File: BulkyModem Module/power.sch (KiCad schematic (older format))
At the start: 15 parts, among them J1 DC IN, J4 Conn_Power, K1 HK19F-DC, U2 74HCT04, U5 74HCT04

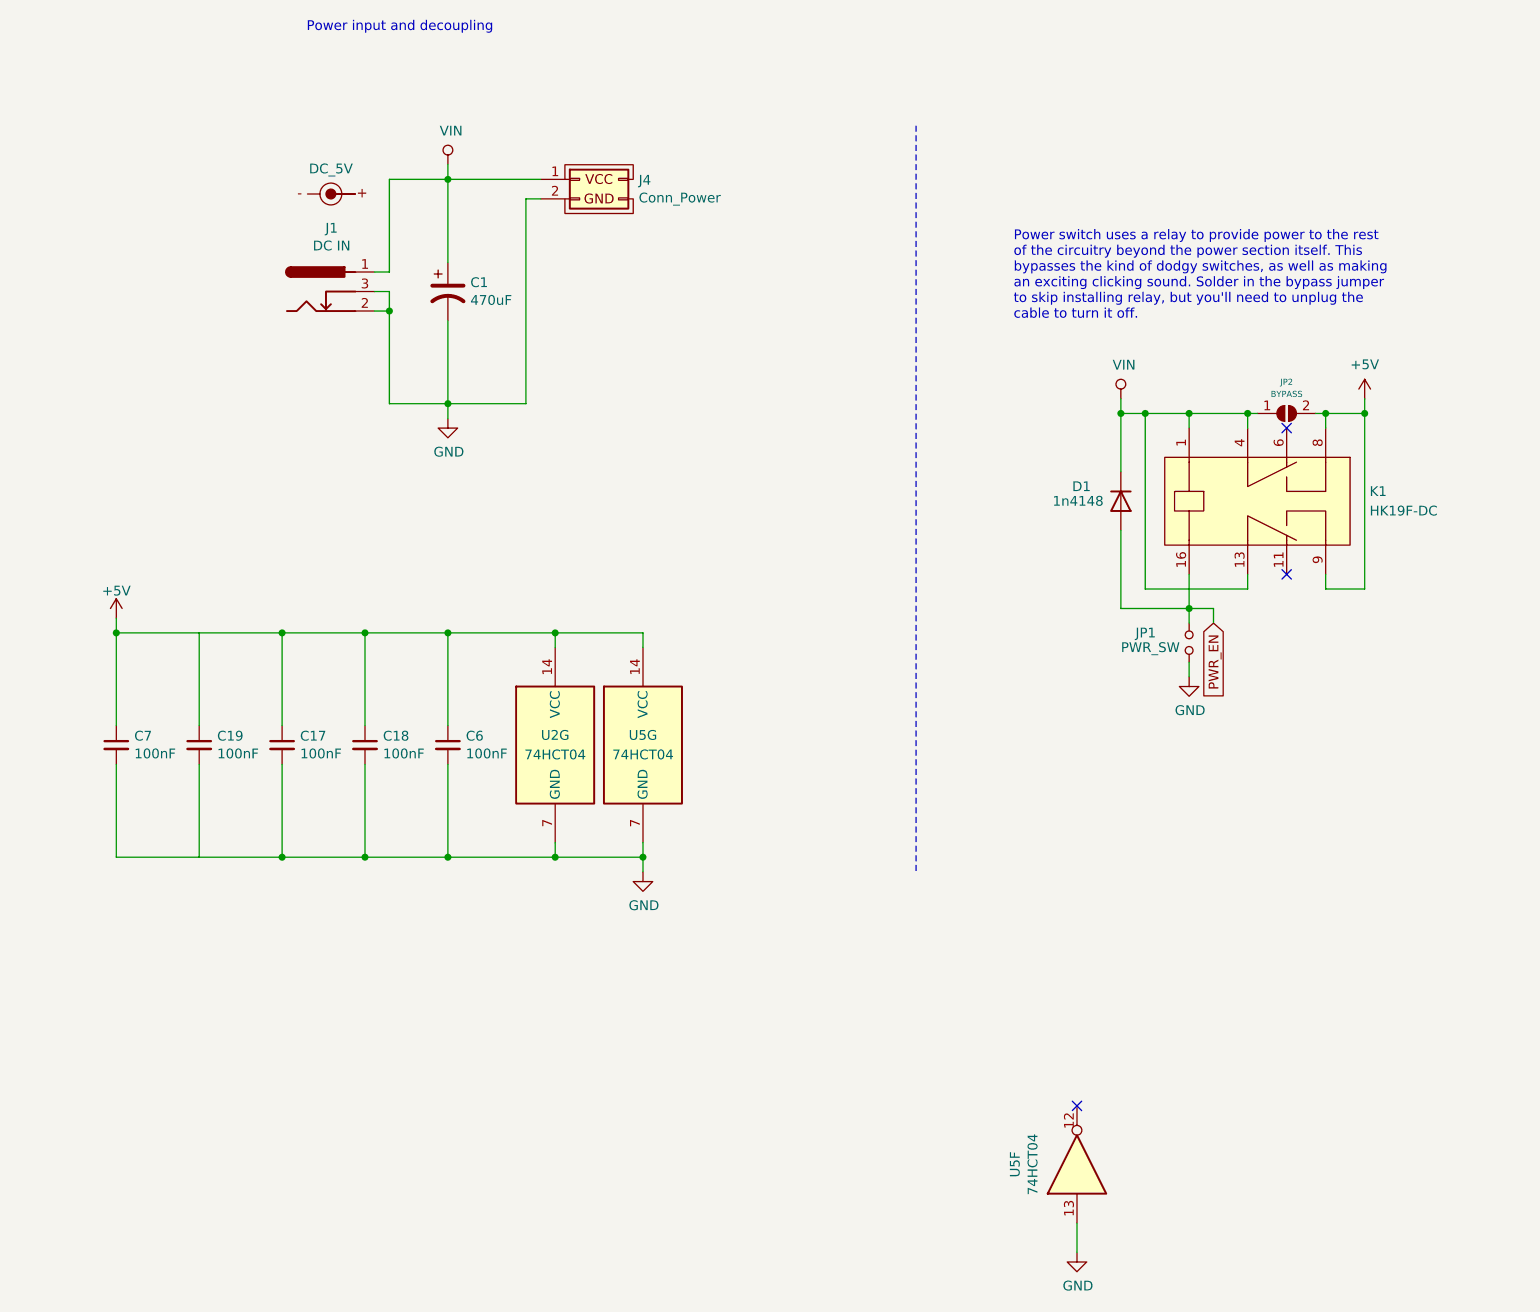
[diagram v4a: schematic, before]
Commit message: Tweak schematic in order to fix LEDs and default jumper settings moved to working configuration
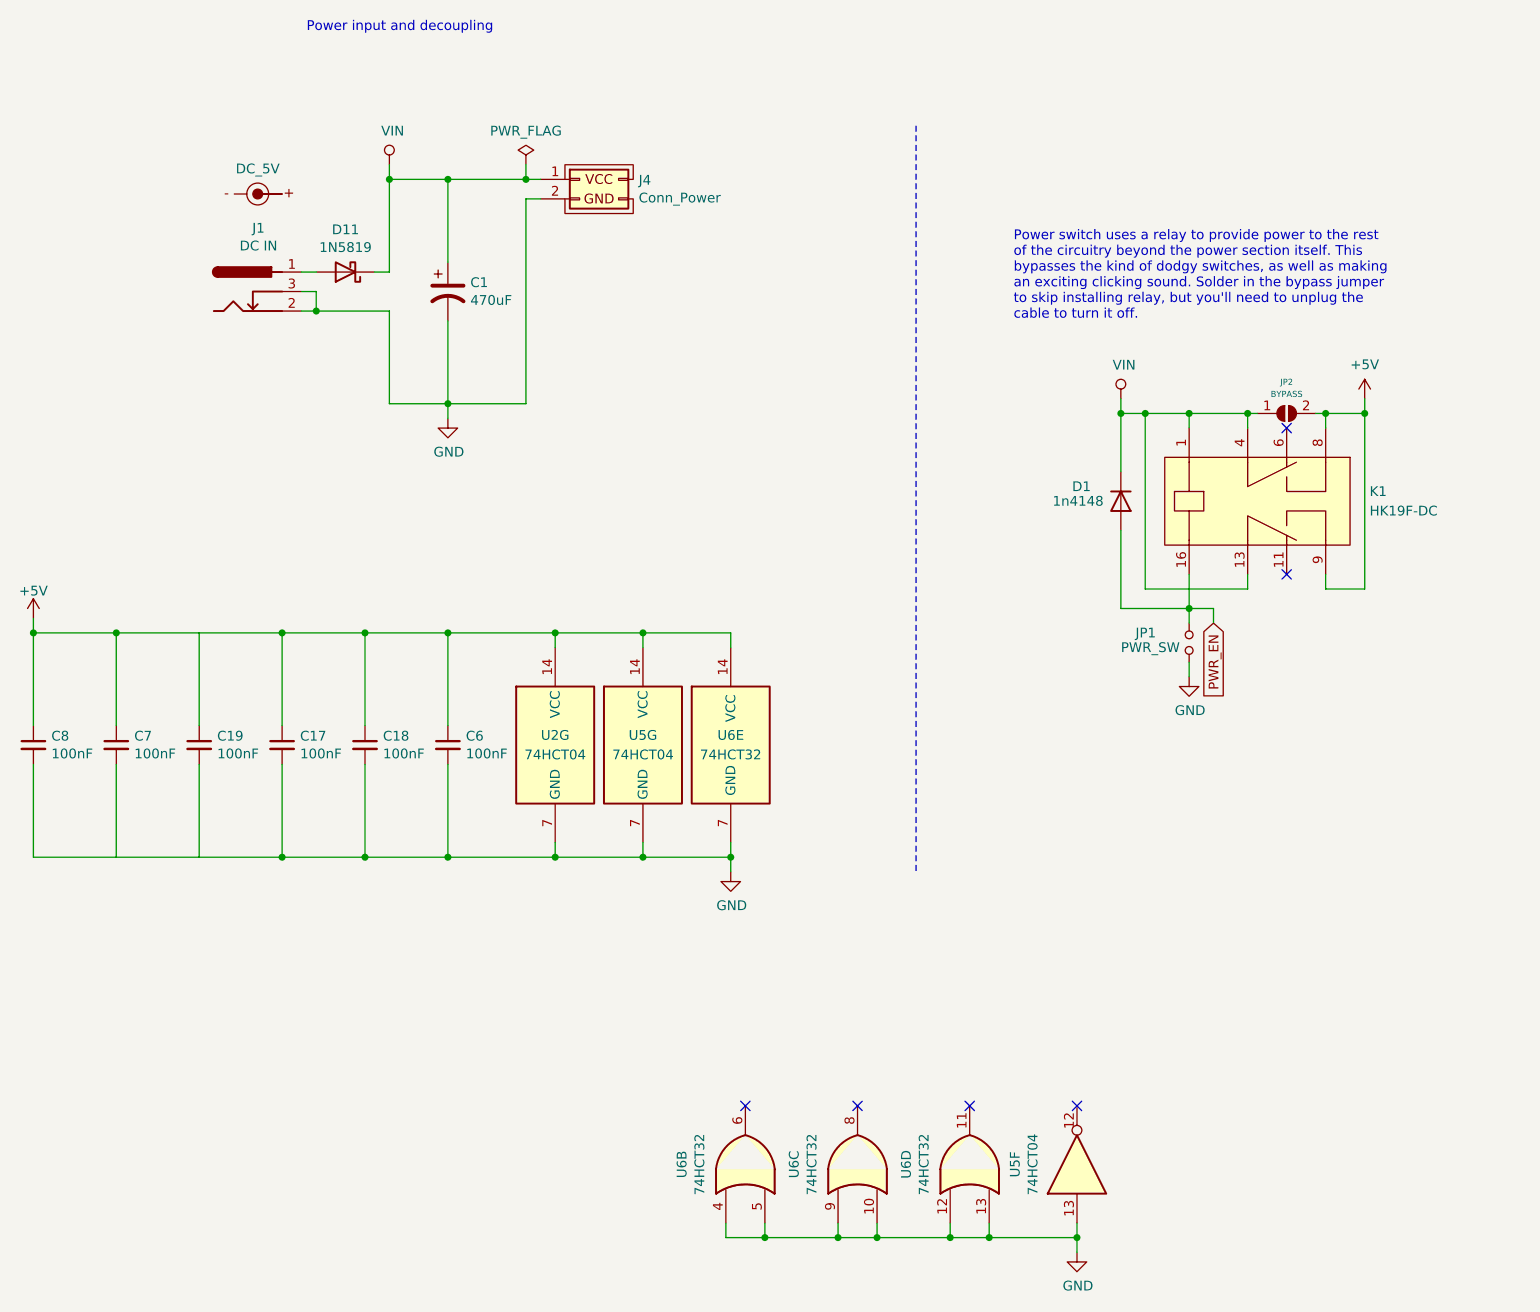
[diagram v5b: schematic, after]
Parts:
- added C8: 100nF, Capacitor_THT:C_Disc_D4.7mm_W2.5mm_P5.00mm, symbol Device:C_Small
- added D11: 1N5819, Diode_THT:D_DO-41_SOD81_P10.16mm_Horizontal, symbol Diode:1N5819
- added U6: 74HCT32, symbol 74xx:74LS32
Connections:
- net +5V: now also C8.1, U6.14 (VCC)
- net GND: now also C8.2, U6.10, U6.12, U6.13, U6.4, U6.5, U6.7 (GND), U6.9
- net VIN: now also D11.1 (K); no longer J1.1
- new net: D11.2 (A), J1.1
- no-connect marks 3 -> 6
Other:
- moved on the sheet: J1
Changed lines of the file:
@@
 Wire Wire Line
 	8125 3125 8125 3200
-Connection ~ 8125 3200
 $Comp
 L Jumper:SolderJumper_2_Open JP?
@@
 L barrel_jack:barrel_9v J?
 U 1 1 63DAB478
-P 2750 2575
+P 2375 2575
 AR Path="/63DAB478" Ref="J?"  Part="1"
 AR Path="/63D786E4/63DAB478" Ref="J1"  Part="1"
-F 0 "J1" H 2829 2900 50  0000 C CNN
-F 1 "DC IN" H 2829 2809 50  0000 C CNN
-F 2 "BulkyModem:BARREL_JACK" H 2800 2535 50  0001 C CNN
-F 3 "~" H 2800 2535 50  0001 C CNN
-	1    2750 2575
+F 0 "J1" H 2454 2900 50  0000 C CNN
+F 1 "DC IN" H 2454 2809 50  0000 C CNN
+F 2 "BulkyModem:BARREL_JACK" H 2425 2535 50  0001 C CNN
+F 3 "~" H 2425 2535 50  0001 C CNN
+	1    2375 2575
 	1    0    0    -1
 $EndComp
@@
 $EndComp
 Wire Wire Line
-	3050 2475 3125 2475
-Wire Wire Line
-	3050 2675 3125 2675
+	2675 2475 2750 2475
+Wire Wire Line
+	2675 2675 2750 2675
 $Comp
 L Device:CP1 C?
@@
 L power:+5V #PWR?
 U 1 1 63DAB492
-P 1725 4250
+P 1300 4250
 AR Path="/63DAB492" Ref="#PWR?"  Part="1"
 AR Path="/63D786E4/63DAB492" Ref="#PWR0110"  Part="1"
-F 0 "#PWR0110" H 1725 4100 50  0001 C CNN
-F 1 "+5V" H 1725 4390 50  0000 C CNN
-F 2 "" H 1725 4250 50  0000 C CNN
-F 3 "" H 1725 4250 50  0000 C CNN
-	1    1725 4250
+F 0 "#PWR0110" H 1300 4100 50  0001 C CNN
+F 1 "+5V" H 1300 4390 50  0000 C CNN
+F 2 "" H 1300 4250 50  0000 C CNN
+F 3 "" H 1300 4250 50  0000 C CNN
+	1    1300 4250
 	1    0    0    -1
 $EndComp
@@
 L power:GND #PWR?
 U 1 1 63DAB499
-P 4425 5550
+P 4875 5550
 AR Path="/63DAB499" Ref="#PWR?"  Part="1"
 AR Path="/63D786E4/63DAB499" Ref="#PWR0133"  Part="1"
-F 0 "#PWR0133" H 4425 5300 50  0001 C CNN
-F 1 "GND" H 4430 5377 50  0000 C CNN
-F 2 "" H 4425 5550 50  0001 C CNN
-F 3 "" H 4425 5550 50  0001 C CNN
-	1    4425 5550
+F 0 "#PWR0133" H 4875 5300 50  0001 C CNN
+F 1 "GND" H 4880 5377 50  0000 C CNN
+F 2 "" H 4875 5550 50  0001 C CNN
+F 3 "" H 4875 5550 50  0001 C CNN
+	1    4875 5550
 	1    0    0    -1
 $EndComp
@@
 	3975 4325 3975 4400
 Wire Wire Line
-	1725 4250 1725 4325
-Wire Wire Line
-	3050 2575 3125 2575
-Wire Wire Line
-	3125 2575 3125 2675
-Connection ~ 3125 2675
-Wire Wire Line
-	3425 1925 3425 2000
+	2675 2575 2750 2575
+Wire Wire Line
+	3125 1925 3125 2000
 Connection ~ 3425 2000
 Wire Wire Line
@@
 	3425 3150 3425 3225
 Wire Wire Line
-	3125 2675 3125 3150
-Wire Wire Line
 	3425 2725 3425 3150
 $Comp
 L BulkyModem:DC_5V SYM?
 U 1 1 63DAB4B1
-P 2825 2075
+P 2450 2075
 AR Path="/63DAB4B1" Ref="SYM?"  Part="1"
 AR Path="/63D786E4/63DAB4B1" Ref="SYM1"  Part="1"
-F 0 "SYM1" H 2825 2296 50  0001 C CNN
-F 1 "DC_5V" H 2825 2204 50  0000 C CNN
-F 2 "BulkyModem:PWR_Specification" H 2700 2175 50  0001 C CNN
-F 3 "" H 2700 2175 50  0001 C CNN
-	1    2825 2075
+F 0 "SYM1" H 2450 2296 50  0001 C CNN
+F 1 "DC_5V" H 2450 2204 50  0000 C CNN
+F 2 "BulkyModem:PWR_Specification" H 2325 2175 50  0001 C CNN
+F 3 "" H 2325 2175 50  0001 C CNN
+	1    2450 2075
 	1    0    0    -1
 $EndComp
@@
 L barrel_jack:VIN #PWR?
 U 1 1 63DAB4BE
-P 3425 1925
+P 3125 1925
 AR Path="/63DAB4BE" Ref="#PWR?"  Part="1"
 AR Path="/63D786E4/63DAB4BE" Ref="#PWR0134"  Part="1"
-F 0 "#PWR0134" H 3425 1775 50  0001 C CNN
-F 1 "VIN" H 3442 2098 50  0000 C CNN
-F 2 "" H 3425 1925 50  0001 C CNN
-F 3 "" H 3425 1925 50  0001 C CNN
-	1    3425 1925
+F 0 "#PWR0134" H 3125 1775 50  0001 C CNN
+F 1 "VIN" H 3142 2098 50  0000 C CNN
+F 2 "" H 3125 1925 50  0001 C CNN
+F 3 "" H 3125 1925 50  0001 C CNN
+	1    3125 1925
 	1    0    0    -1
 $EndComp
@@
 	3975 4325 3425 4325
 Wire Wire Line
-	4425 5550 4425 5475
+	4875 5550 4875 5475
 Connection ~ 3975 5475
 Text Notes 6325 2725 0    50   ~ 0
@@
 	3825 3150 3425 3150
 Wire Wire Line
-	3425 2000 3900 2000
+	3425 2000 3825 2000
 Wire Wire Line
 	3125 2000 3425 2000
@@
 	1    0    0    -1
 $EndComp
-Connection ~ 4425 5475
 $Comp
 L Device:C_Small C?
@@
 Wire Wire Line
 	1725 4325 2150 4325
+Wire Wire Line
+	6650 7350 6650 7425
+$Comp
+L Diode:1N5819 D11
+U 1 1 644AC11F
+P 2900 2475
+F 0 "D11" H 2900 2258 50  0000 C CNN
+F 1 "1N5819" H 2900 2349 50  0000 C CNN
+F 2 "Diode_THT:D_DO-41_SOD81_P10.16mm_Horizontal" H 2900 2300 50  0001 C CNN
+F 3 "http://www.vishay.com/docs/88525/1n5817.pdf" H 2900 2475 50  0001 C CNN
+	1    2900 2475
+	-1   0    0    1
+$EndComp
+Connection ~ 8125 3200
+Wire Wire Line
+	3125 2475 3050 2475
+Wire Wire Line
+	2750 2675 2750 2575
+Wire Wire Line
+	2750 2675 3125 2675
+Connection ~ 2750 2675
+Wire Wire Line
+	3125 2675 3125 3150
+$Comp
+L power:PWR_FLAG #FLG0101
+U 1 1 64522A66
+P 3825 1925
+F 0 "#FLG0101" H 3825 2000 50  0001 C CNN
+F 1 "PWR_FLAG" H 3825 2098 50  0000 C CNN
+F 2 "" H 3825 1925 50  0001 C CNN
+F 3 "~" H 3825 1925 50  0001 C CNN
+	1    3825 1925
+	1    0    0    -1
+$EndComp
+Wire Wire Line
+	3825 1925 3825 2000
+Connection ~ 3825 2000
+Wire Wire Line
+	3825 2000 3900 2000
+Connection ~ 3125 2000
+$Comp
+L 74xx:74LS32 U6
+U 5 1 64571FD8
+P 4875 4900
+F 0 "U6" H 4875 4950 50  0000 C CNN
+F 1 "74HCT32" H 4875 4850 50  0000 C CNN
+F 2 "" H 4875 4900 50  0001 C CNN
+F 3 "http://www.ti.com/lit/gpn/sn74LS32" H 4875 4900 50  0001 C CNN
+	5    4875 4900
+	1    0    0    -1
+$EndComp
+Wire Wire Line
+	4425 4325 4875 4325
+Wire Wire Line
+	4875 4325 4875 4400
+Connection ~ 4425 4325
+Wire Wire Line
+	4875 5475 4425 5475
+Connection ~ 4425 5475
+Wire Wire Line
+	4875 5400 4875 5475
+Connection ~ 4875 5475
+$Comp
+L 74xx:74LS32 U6
+U 2 1 64584572
+P 4950 7050
+F 0 "U6" H 4950 7375 50  0000 C CNN
+F 1 "74HCT32" H 4950 7284 50  0000 C CNN
+F 2 "" H 4950 7050 50  0001 C CNN
+F 3 "http://www.ti.com/lit/gpn/sn74LS32" H 4950 7050 50  0001 C CNN
+	2    4950 7050
+	0    -1   -1   0
+$EndComp
+$Comp
+L 74xx:74LS32 U6
+U 3 1 6458571D
+P 5525 7050
+F 0 "U6" H 5525 7375 50  0000 C CNN
+F 1 "74HCT32" H 5525 7284 50  0000 C CNN
+F 2 "" H 5525 7050 50  0001 C CNN
+F 3 "http://www.ti.com/lit/gpn/sn74LS32" H 5525 7050 50  0001 C CNN
+	3    5525 7050
+	0    -1   -1   0
+$EndComp
+$Comp
+L 74xx:74LS32 U6
+U 4 1 6458699B
+P 6100 7050
+F 0 "U6" H 6100 7375 50  0000 C CNN
+F 1 "74HCT32" H 6100 7284 50  0000 C CNN
+F 2 "" H 6100 7050 50  0001 C CNN
+F 3 "http://www.ti.com/lit/gpn/sn74LS32" H 6100 7050 50  0001 C CNN
+	4    6100 7050
+	0    -1   -1   0
+$EndComp
+Wire Wire Line
+	6650 7425 6200 7425
+Wire Wire Line
+	4850 7425 4850 7350
+Connection ~ 6650 7425
+Wire Wire Line
+	6650 7425 6650 7500
+Wire Wire Line
+	5050 7350 5050 7425
+Connection ~ 5050 7425
+Wire Wire Line
+	5050 7425 4850 7425
+Wire Wire Line
+	5425 7350 5425 7425
+Connection ~ 5425 7425
+Wire Wire Line
+	5425 7425 5050 7425
+Wire Wire Line
+	5625 7350 5625 7425
+Connection ~ 5625 7425
+Wire Wire Line
+	5625 7425 5425 7425
+Wire Wire Line
+	6000 7350 6000 7425
+Connection ~ 6000 7425
+Wire Wire Line
+	6000 7425 5625 7425
+Wire Wire Line
+	6200 7350 6200 7425
+Connection ~ 6200 7425
+Wire Wire Line
+	6200 7425 6000 7425
+NoConn ~ 4950 6750
+NoConn ~ 5525 6750
+NoConn ~ 6100 6750
+$Comp
+L Device:C_Small C?
+U 1 1 64802B72
+P 1300 4900
+AR Path="/64802B72" Ref="C?"  Part="1"
+AR Path="/63D786E4/64802B72" Ref="C8"  Part="1"
+F 0 "C8" H 1392 4946 50  0000 L CNN
+F 1 "100nF" H 1392 4855 50  0000 L CNN
+F 2 "Capacitor_THT:C_Disc_D4.7mm_W2.5mm_P5.00mm" H 1300 4900 50  0001 C CNN
+F 3 "~" H 1300 4900 50  0001 C CNN
+	1    1300 4900
+	1    0    0    -1
+$EndComp
+Wire Wire Line
+	1300 5000 1300 5475
+Wire Wire Line
+	1300 5475 1725 5475
+Wire Wire Line
+	1300 4250 1300 4325
+Wire Wire Line
+	1725 4325 1300 4325
 Connection ~ 1725 4325
-Wire Wire Line
-	6650 7350 6650 7500
+Connection ~ 1300 4325
+Wire Wire Line
+	1300 4325 1300 4800
 $EndSCHEMATC

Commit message: Layout updated
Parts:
- removed J4: Conn_Power, BulkyModem:Conn_Power, symbol BulkyModem:Conn_Power
- added D12: STANDBY, LED_THT:LED_D3.0mm, symbol Device:LED
- added R1: 2k2, resistor:R_Axial_DIN0207_L6.3mm_D2.5mm_P10.16mm_Horizontal, symbol Device:R
- U6: footprint (none) -> Package_DIP:DIP-14_W7.62mm_Socket_LongPads
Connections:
- net GND: now also R1.1
- net VSB: now reaches K1.11 (NC_2)
- net VSB: now also D12.2 (A)
- new net: D12.1 (K), R1.2
- no-connect marks 6 -> 5
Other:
- moved on the sheet: JP2

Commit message: Revised version. Mainly buffering signals
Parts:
- removed unit 2 of U6
- removed unit 3 of U6
- J1: symbol barrel_jack:barrel_9v -> barrel_jack:Jack-DC
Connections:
- no-connect marks 5 -> 3
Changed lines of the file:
@@
-$Comp
-L 74xx:74LS32 U6
-U 2 1 64584572
-P 4950 7050
-F 0 "U6" H 4950 7375 50  0000 C CNN
-F 1 "74HCT32" H 4950 7284 50  0000 C CNN
-F 2 "Package_DIP:DIP-14_W7.62mm_Socket_LongPads" H 4950 7050 50  0001 C CNN
-F 3 "http://www.ti.com/lit/gpn/sn74LS32" H 4950 7050 50  0001 C CNN
-	2    4950 7050
-	0    -1   -1   0
-$EndComp
-$Comp
-L 74xx:74LS32 U6
-U 3 1 6458571D
-P 5525 7050
-F 0 "U6" H 5525 7375 50  0000 C CNN
-F 1 "74HCT32" H 5525 7284 50  0000 C CNN
-F 2 "Package_DIP:DIP-14_W7.62mm_Socket_LongPads" H 5525 7050 50  0001 C CNN
-F 3 "http://www.ti.com/lit/gpn/sn74LS32" H 5525 7050 50  0001 C CNN
-	3    5525 7050
-	0    -1   -1   0
-$EndComp
 $Comp
 L 74xx:74LS32 U6
@@
 Wire Wire Line
 	6650 7425 6200 7425
-Wire Wire Line
-	4850 7425 4850 7350
 Connection ~ 6650 7425
 Wire Wire Line
 	6650 7425 6650 7500
 Wire Wire Line
-	5050 7350 5050 7425
-Connection ~ 5050 7425
-Wire Wire Line
-	5050 7425 4850 7425
-Wire Wire Line
-	5425 7350 5425 7425
-Connection ~ 5425 7425
-Wire Wire Line
-	5425 7425 5050 7425
-Wire Wire Line
-	5625 7350 5625 7425
-Connection ~ 5625 7425
-Wire Wire Line
-	5625 7425 5425 7425
-Wire Wire Line
 	6000 7350 6000 7425
-Connection ~ 6000 7425
-Wire Wire Line
-	6000 7425 5625 7425
 Wire Wire Line
 	6200 7350 6200 7425
@@
 Wire Wire Line
 	6200 7425 6000 7425
-NoConn ~ 4950 6750
-NoConn ~ 5525 6750
 NoConn ~ 6100 6750
 $Comp
@@
 	2675 2475 2750 2475
 $Comp
-L barrel_jack:barrel_9v J?
+L barrel_jack:Jack-DC J?
 U 1 1 63DAB478
 P 2375 2575

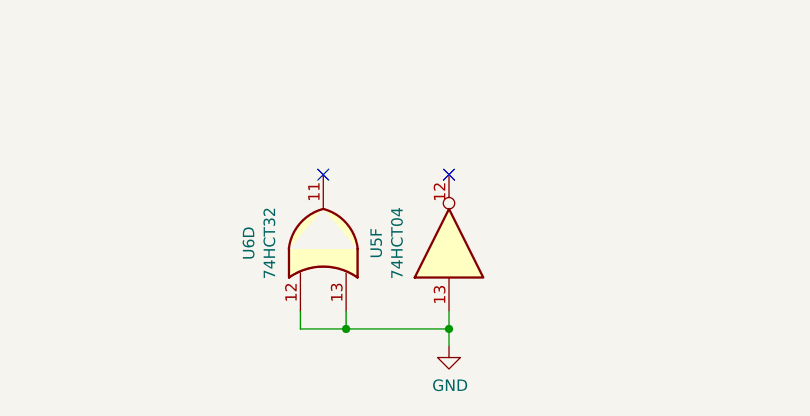
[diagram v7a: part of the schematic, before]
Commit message: Tweaks needed to make revision C actually work.
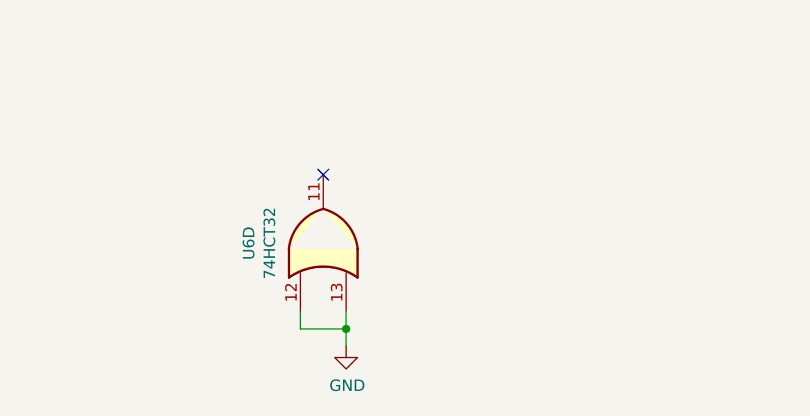
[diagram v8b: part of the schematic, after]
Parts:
- removed unit 6 of U5
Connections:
- no-connect marks 3 -> 2
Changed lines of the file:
@@
 	4425 5475 3975 5475
-$Comp
-L 74xx:74HCT04 U?
-U 6 1 63275CC3
-P 6650 7050
-AR Path="/63275CC3" Ref="U?"  Part="1"
-AR Path="/6390AE73/63275CC3" Ref="U?"  Part="1"
-AR Path="/63D786E4/63275CC3" Ref="U5"  Part="6"
-F 0 "U5" H 6650 7367 50  0000 C CNN
-F 1 "74HCT04" H 6650 7276 50  0000 C CNN
-F 2 "Package_DIP:DIP-14_W7.62mm_Socket_LongPads" H 6650 7050 50  0001 C CNN
-F 3 "https://assets.nexperia.com/documents/data-sheet/74HC_HCT04.pdf" H 6650 7050 50  0001 C CNN
-	6    6650 7050
-	0    -1   -1   0
-$EndComp
-NoConn ~ 6650 6750
 $Comp
 L power:GND #PWR?
 U 1 1 632A80BC
-P 6650 7500
+P 6200 7500
 AR Path="/632A80BC" Ref="#PWR?"  Part="1"
 AR Path="/63D786E4/632A80BC" Ref="#PWR0105"  Part="1"
-F 0 "#PWR0105" H 6650 7250 50  0001 C CNN
-F 1 "GND" H 6655 7327 50  0000 C CNN
-F 2 "" H 6650 7500 50  0001 C CNN
-F 3 "" H 6650 7500 50  0001 C CNN
-	1    6650 7500
+F 0 "#PWR0105" H 6200 7250 50  0001 C CNN
+F 1 "GND" H 6205 7327 50  0000 C CNN
+F 2 "" H 6200 7500 50  0001 C CNN
+F 3 "" H 6200 7500 50  0001 C CNN
+	1    6200 7500
 	1    0    0    -1
 $EndComp
@@
 Wire Wire Line
 	1725 4325 2150 4325
-Wire Wire Line
-	6650 7350 6650 7425
 Connection ~ 8125 3050
 $Comp
@@
 $EndComp
 Wire Wire Line
-	6650 7425 6200 7425
-Connection ~ 6650 7425
-Wire Wire Line
-	6650 7425 6650 7500
+	6200 7425 6200 7500
 Wire Wire Line
 	6000 7350 6000 7425
